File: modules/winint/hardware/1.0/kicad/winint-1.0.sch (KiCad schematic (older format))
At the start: 56 parts, among them J1 Screw_Terminal_01x09, J2 Screw_Terminal_01x09, J3 M12-5PIN, J4 RELAYS, K1 SANYOU_SRD_Form_C, K2 SANYOU_SRD_Form_C, Q1 2N2219, Q2 2N2219, SW1 INSTANCE, U1 ROT, U2 DOK, U3 STP, U4 DEP, U5 RET, U6 OVL, U7 Teensy_3.2, U8 TEC2-2411WI, U9 MCP2551-I-P

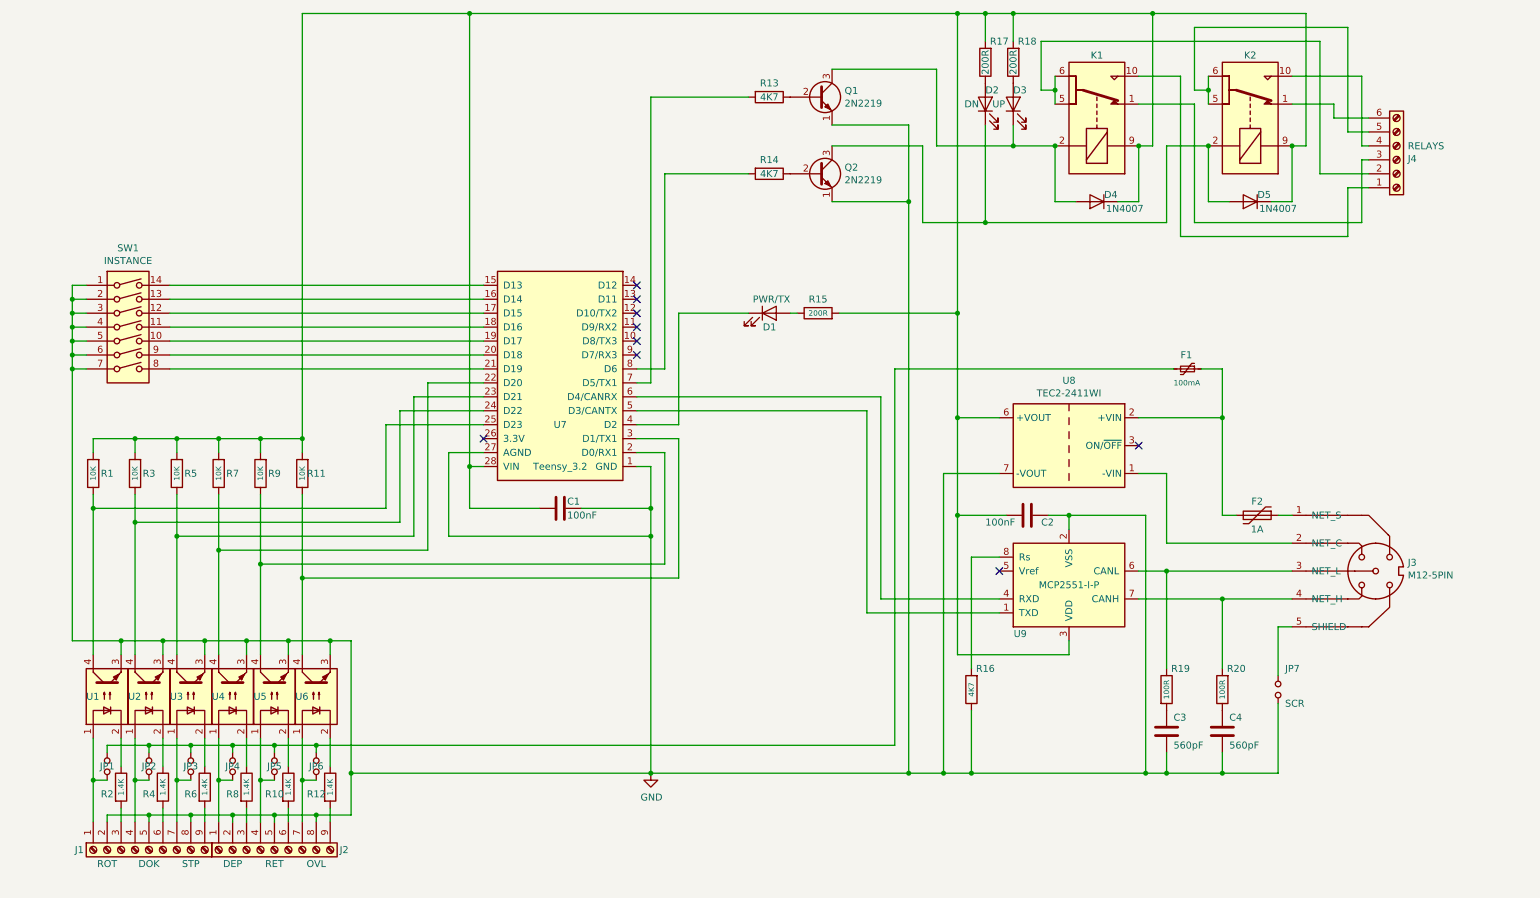
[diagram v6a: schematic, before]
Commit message: Diode protection on sensor supply
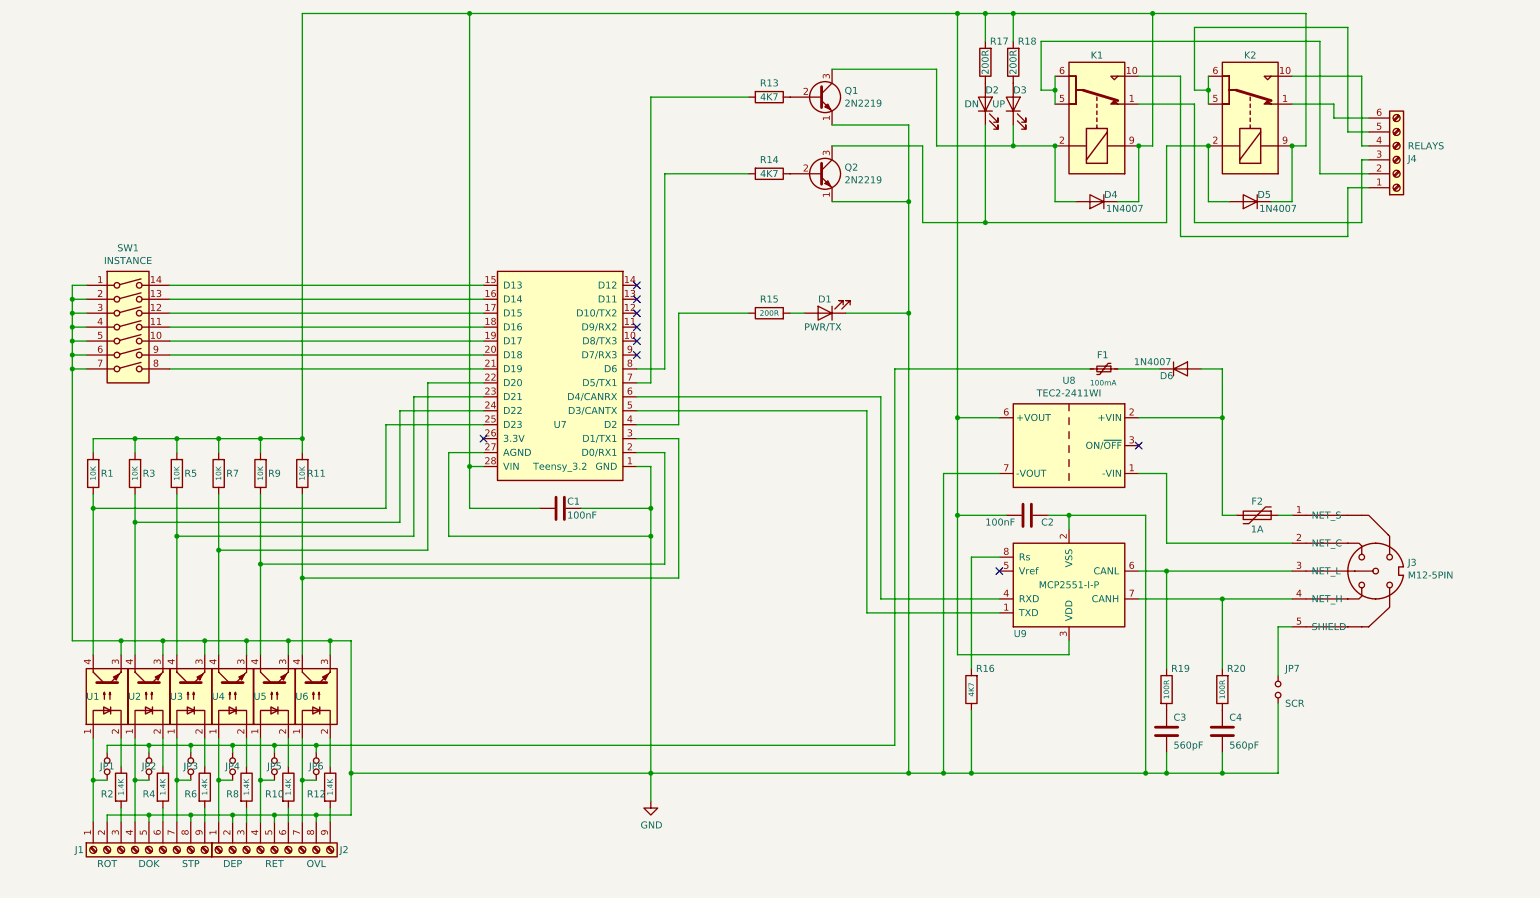
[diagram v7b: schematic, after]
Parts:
- added D6: 1N4007, Diode_THT:D_DO-41_SOD81_P7.62mm_Horizontal, symbol Diode:1N4007
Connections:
- net GND: now also D1.1 (K)
- net at C1.1, C2.1, D4.1 (K)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: no longer R15.2
- net at F2.2, U8.2 (+VIN): now also D6.2 (A); no longer F1.1
- net at R15.1: now also U7.4 (D2); no longer D1.2 (A)
- new net: D6.1 (K), F1.1
- new net: D1.2 (A), R15.2
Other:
- moved on the sheet: D1, F1, R15
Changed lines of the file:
@@
 Wire Wire Line
 	7050 1150 6300 1150
-Wire Wire Line
-	7200 3650 7200 2900
 Connection ~ 7200 3650
 $Comp
 L Device:Polyfuse_Small F1
 U 1 1 5F1D6762
-P 8850 3300
-F 0 "F1" V 8750 3250 50  0000 L CNN
-F 1 "100mA" V 8950 3200 39  0000 L CNN
-F 2 "Fuse:Fuse_Littelfuse_395Series" H 8900 3100 50  0001 L CNN
-F 3 "~" H 8850 3300 50  0001 C CNN
-	1    8850 3300
+P 8250 3300
+F 0 "F1" V 8150 3250 50  0000 L CNN
+F 1 "100mA" V 8350 3200 39  0000 L CNN
+F 2 "Fuse:Fuse_Littelfuse_395Series" H 8300 3100 50  0001 L CNN
+F 3 "~" H 8250 3300 50  0001 C CNN
+	1    8250 3300
 	0    1    1    0
 $EndComp
@@
 Connection ~ 6850 2100
 Wire Wire Line
-	6850 2100 6850 6200
+	6850 2100 6850 2900
 Connection ~ 6850 6200
 Wire Wire Line
@@
 L Device:R R15
 U 1 1 5F2B75CF
-P 6200 2900
-F 0 "R15" V 6300 2900 50  0000 C CNN
-F 1 "200R" V 6200 2900 39  0000 C CNN
-F 2 "Resistor_THT:R_Axial_DIN0204_L3.6mm_D1.6mm_P5.08mm_Horizontal" V 6130 2900 50  0001 C CNN
-F 3 "~" H 6200 2900 50  0001 C CNN
-F 4 "0.125W" V 6300 2900 50  0001 C CNN "Power"
-	1    6200 2900
-	0    -1   -1   0
-$EndComp
-Wire Wire Line
-	6350 2900 7200 2900
+P 5850 2900
+F 0 "R15" V 5950 2900 50  0000 C CNN
+F 1 "200R" V 5850 2900 39  0000 C CNN
+F 2 "Resistor_THT:R_Axial_DIN0204_L3.6mm_D1.6mm_P5.08mm_Horizontal" V 5780 2900 50  0001 C CNN
+F 3 "~" H 5850 2900 50  0001 C CNN
+F 4 "0.125W" V 5950 2900 50  0001 C CNN "Power"
+	1    5850 2900
+	0    -1   -1   0
+$EndComp
 $Comp
 L Device:Polyfuse F2
@@
 L Device:LED D1
 U 1 1 5F3B6D27
-P 5850 2900
-F 0 "D1" H 5900 2800 50  0000 R CNN
-F 1 "PWR/TX" H 6000 3000 50  0000 R CNN
-F 2 "LED_THT:LED_D3.0mm" H 5850 2900 50  0001 C CNN
-F 3 "~" H 5850 2900 50  0001 C CNN
-	1    5850 2900
-	1    0    0    -1
+P 6250 2900
+F 0 "D1" H 6300 2800 50  0000 R CNN
+F 1 "PWR/TX" H 6400 3000 50  0000 R CNN
+F 2 "LED_THT:LED_D3.0mm" H 6250 2900 50  0001 C CNN
+F 3 "~" H 6250 2900 50  0001 C CNN
+	1    6250 2900
+	-1   0    0    1
 $EndComp
 $Comp
@@
 	2600 6000 2600 6050
 Connection ~ 2300 6000
-Connection ~ 2600 6000
 $Comp
 L Device:R R2
@@
 Wire Wire Line
 	5100 1900 5700 1900
-Connection ~ 7200 2900
-Wire Wire Line
-	7200 750  7200 2900
 Wire Wire Line
 	5700 2900 5200 2900
 Wire Wire Line
-	6000 2900 6050 2900
-Wire Wire Line
-	8750 3300 6750 3300
-Wire Wire Line
-	2600 6000 6750 6000
+	8150 3300 6750 3300
 Wire Wire Line
 	6750 3300 6750 6000
@@
 L power:GND #PWR0101
 U 1 1 5FD8D24E
-P 5000 6200
-F 0 "#PWR0101" H 5000 5950 50  0001 C CNN
-F 1 "GND" H 5005 6027 50  0000 C CNN
-F 2 "" H 5000 6200 50  0001 C CNN
-F 3 "" H 5000 6200 50  0001 C CNN
-	1    5000 6200
+P 5000 6400
+F 0 "#PWR0101" H 5000 6150 50  0001 C CNN
+F 1 "GND" H 5005 6227 50  0000 C CNN
+F 2 "" H 5000 6400 50  0001 C CNN
+F 3 "" H 5000 6400 50  0001 C CNN
+	1    5000 6400
 	1    0    0    -1
 $EndComp
@@
 Wire Wire Line
 	850  3300 850  5250
+Wire Wire Line
+	5000 6400 5000 6200
+$Comp
+L Diode:1N4007 D6
+U 1 1 5FC2E5E3
+P 8800 3300
+F 0 "D6" H 8700 3250 50  0000 C CNN
+F 1 "1N4007" H 8600 3350 50  0000 C CNN
+F 2 "Diode_THT:D_DO-41_SOD81_P7.62mm_Horizontal" H 8800 3125 50  0001 C CNN
+F 3 "http://www.vishay.com/docs/88503/1n4001.pdf" H 8800 3300 50  0001 C CNN
+	1    8800 3300
+	1    0    0    -1
+$EndComp
+Connection ~ 2600 6000
+Wire Wire Line
+	2600 6000 6750 6000
+Wire Wire Line
+	8350 3300 8650 3300
+Wire Wire Line
+	7200 750  7200 3650
+Wire Wire Line
+	6400 2900 6850 2900
+Connection ~ 6850 2900
+Wire Wire Line
+	6850 2900 6850 6200
+Wire Wire Line
+	6000 2900 6100 2900
 $EndSCHEMATC

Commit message: Added snubber circuit to relay NO output
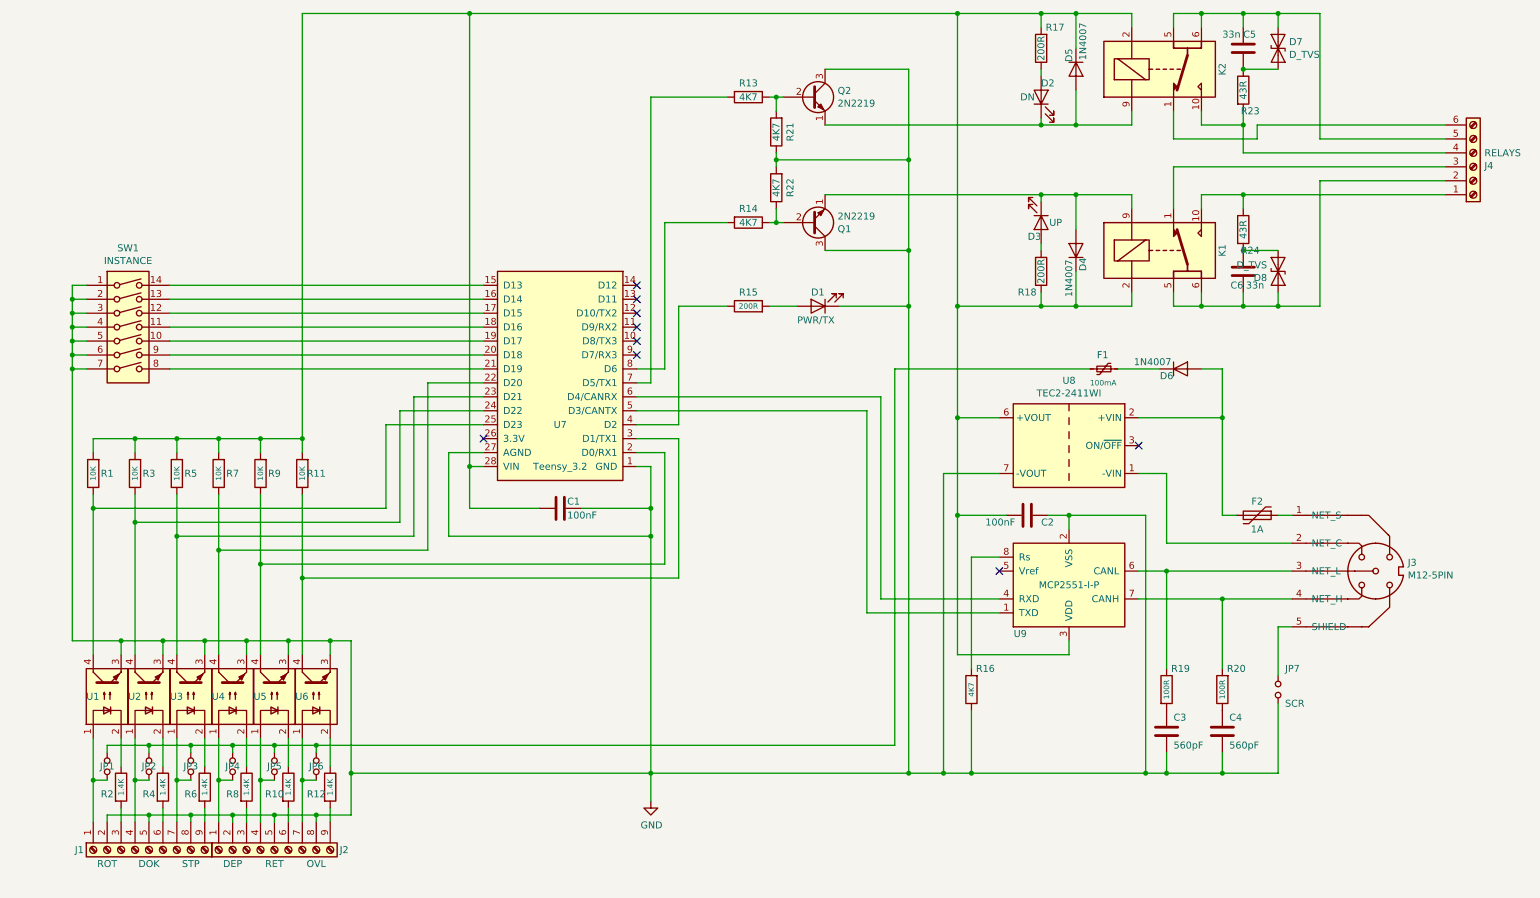
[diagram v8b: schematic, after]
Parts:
- added C5, C6: 33n, Capacitor_THT:CP_Radial_D5.0mm_P2.50mm, symbol Device:C
- added D7, D8: D_TVS, Diode_THT:D_DO-27_P5.08mm_Vertical_AnodeUp, symbol Device:D_TVS
- added R21, R22: 4K7, Resistor_THT:R_Axial_DIN0204_L3.6mm_D1.6mm_P5.08mm_Horizontal, symbol Device:R
- added R23, R24: 43R, Resistor_THT:R_Axial_DIN0204_L3.6mm_D1.6mm_P5.08mm_Horizontal, symbol Device:R
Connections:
- net GND: now also Q1.3 (C), Q2.3 (C), R21.1, R22.2; no longer Q1.1 (E), Q2.1 (E)
- net at C1.1, C2.1, D4.1 (K)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: now also K1.2, K2.2; no longer K1.9, K2.9
- net at Q1.2 (B): now also R14.1, R22.1; no longer R13.1
- net at D3.1 (K), D4.2 (A): now also K1.9, Q1.1 (E); no longer K1.2, Q1.3 (C)
- net at J4.1 (Pin_1), K1.10: now also R24.1
- net at J4.2 (Pin_2), K1.5, K1.6: now also C6.2, D8.1 (A1)
- net at J4.4 (Pin_4), K2.10: now also R23.2
- net at J4.5 (Pin_5), K2.5, K2.6: now also C5.2, D7.1 (A1)
- net at Q2.2 (B): now also R13.1, R21.2; no longer R14.1
- net at D2.1 (K), D5.2 (A): now also K2.9, Q2.1 (E); no longer K2.2, Q2.3 (C)
- new net: C5.1, D7.2 (A2), R23.1
- new net: C6.1, D8.2 (A2), R24.2
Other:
- moved on the sheet: D1, D2, D3, D4, D5, J4, K1, K2, Q1, Q2, R13, R14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
